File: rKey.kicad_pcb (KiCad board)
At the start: 2 copper layers, 52.8 x 71.4 mm, 38 parts, among them IC1 BDX34C, J1 Conn_01x06, Q1 BC337, Q2 BC337, Q3 BC337, Q4 BC337, Q5 BC327, Q8 BC337, U1 TL084BCN, U2 LM7810_TO220

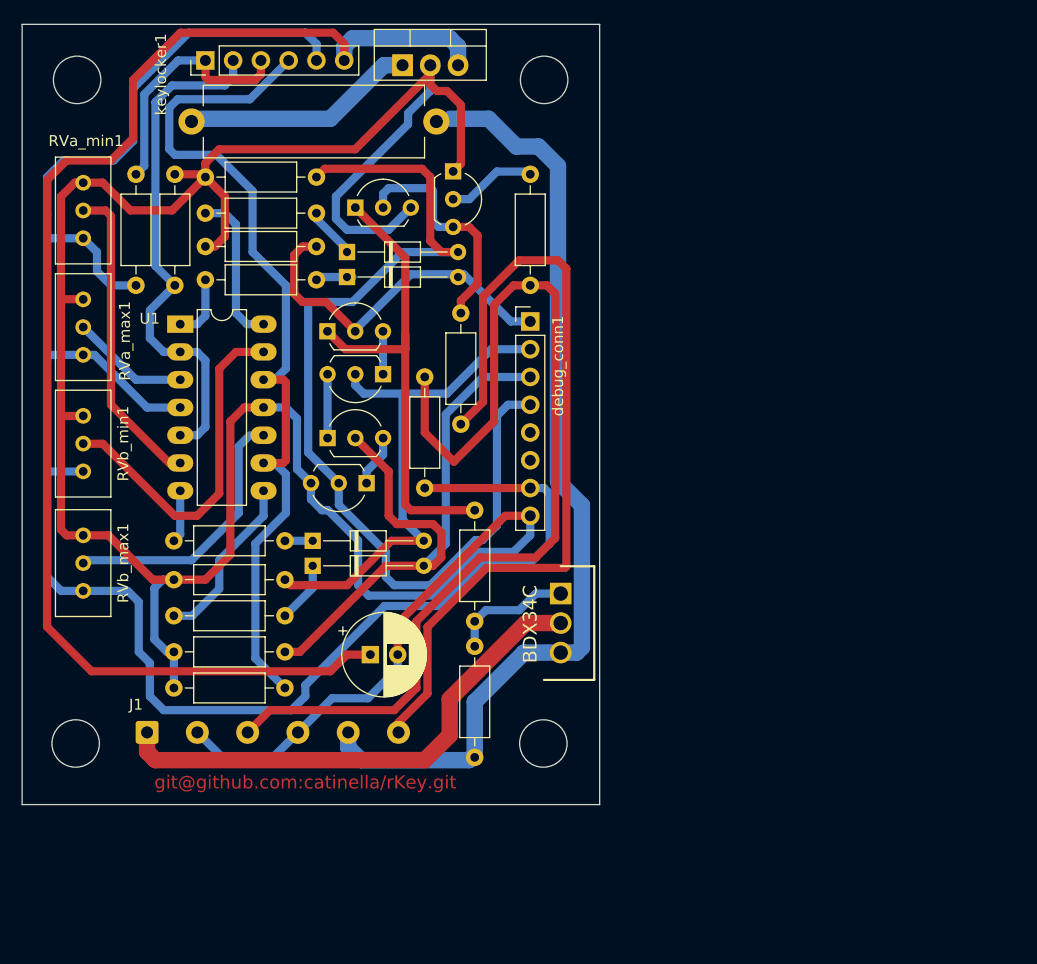
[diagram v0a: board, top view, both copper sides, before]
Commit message: Fix: Zenner diode added
To allow the STOP button to turn off the services' controller, the Zenner has been placed between the ON status holdon pin
and its BC327 transistor. When you stop the engine your key must be not plugged, obviosely.
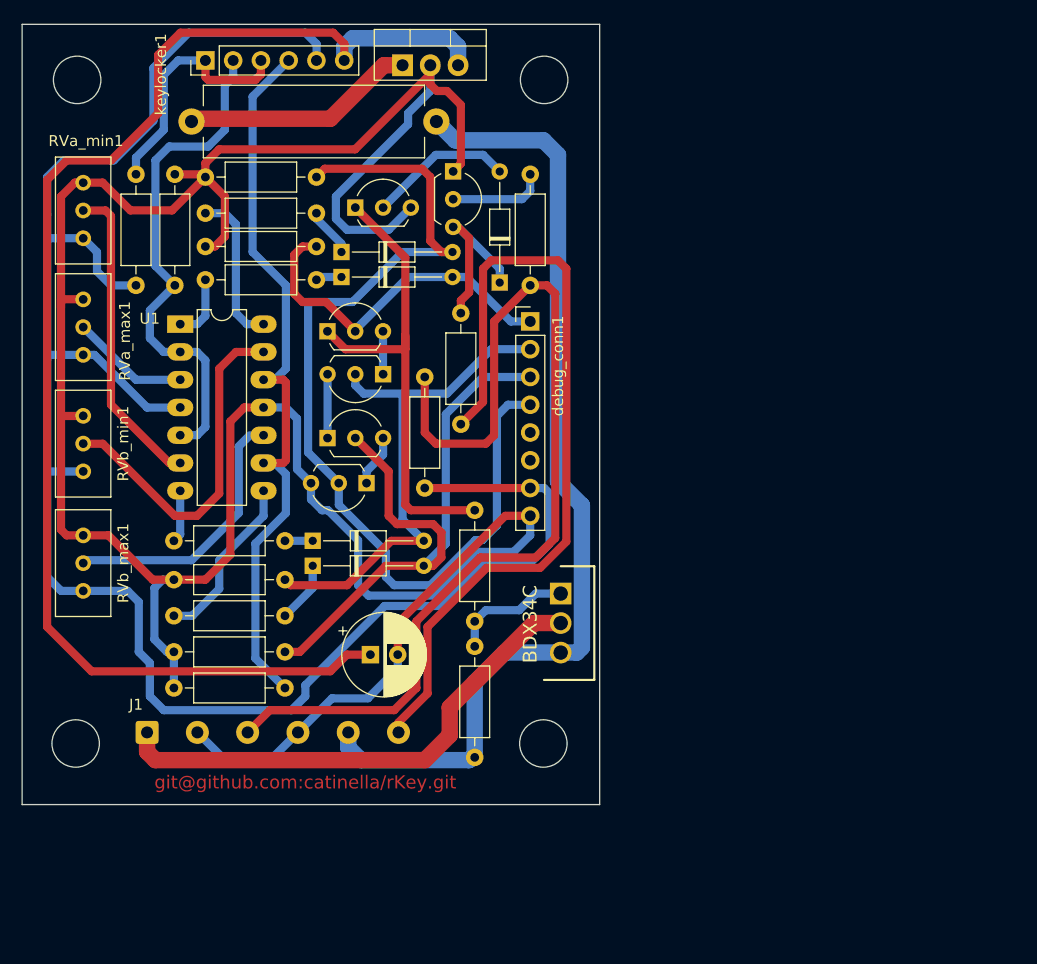
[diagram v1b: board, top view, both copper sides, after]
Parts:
- added ZD1: 2V, Diode_THT:D_DO-34_SOD68_P10.16mm_Horizontal, F.Cu at (160.3, 80.3)
- moved ZD4 0.51 mm to (145.8, 77.5)
- moved ZD5 0.51 mm to (145.8, 79.8)
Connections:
- Q5 pad 3: Net-(Q8-Pad2) -> Net-(R9-Pad1)
- R9 pad 1: Net-(Q8-Pad2) -> Net-(R9-Pad1)
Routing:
- net Net-(R9-Pad1): track 0.00 -> 16.2 mm
- net Net-(R8-Pad1): track 81.4 -> 69.0 mm
- net Net-(Q8-Pad2): track 21.3 -> 13.3 mm
- net Net-(IC1-Pad3): track 87.0 -> 89.7 mm
- net Net-(J1-Pad3): track 92.8 -> 91.3 mm
- net Net-(R2-Pad2): track 3.41 -> 2.39 mm
- net Net-(Q4-Pad2): track 89.8 -> 88.8 mm
- net Net-(R7-Pad1): track 47.5 -> 46.7 mm
- net Net-(R13-Pad1): track 8.21 -> 8.89 mm

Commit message: Release based on two D45VH10 (10A --> 3W) 2.5% wasted power
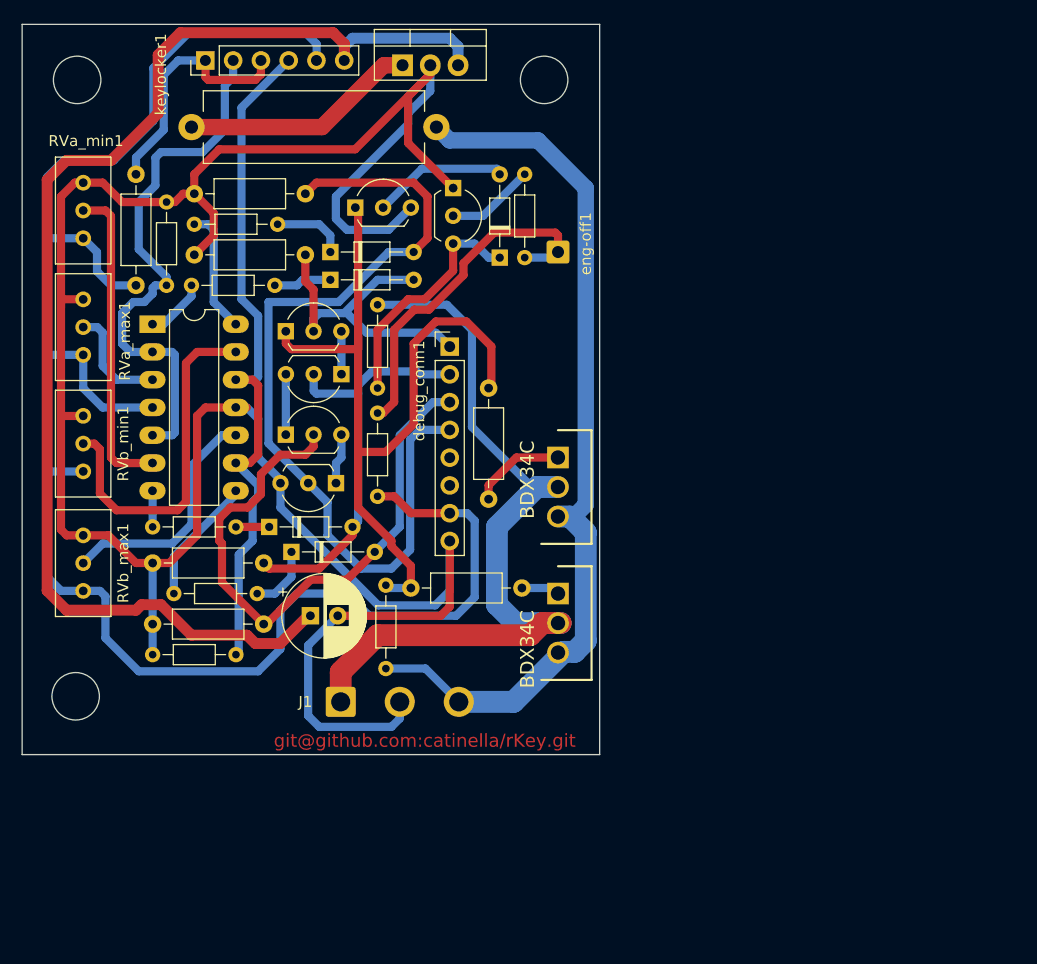
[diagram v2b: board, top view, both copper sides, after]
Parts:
- added IC2: BDX34C, BDX34C:TO270P460X1020X2008-3P, F.Cu at (165.6, 96.3)
- added R18: 1.6K, Resistor_THT:R_Axial_DIN0207_L6.3mm_D2.5mm_P10.16mm_Horizontal, F.Cu at (159.3, 89.9)
- added eng-off1: Conn_01x01, Connector_Wire:SolderWire-0.5sqmm_1x01_D0.9mm_OD2.1mm, F.Cu at (165.6, 77.5)
- J1: value Conn_01x06 -> Conn_01x03; footprint Connector_Wire:SolderWire-0.5sqmm_1x06_P4.6mm_D0.9mm_OD2.1mm -> Connector_Wire:SolderWire-1sqmm_1x03_P5.4mm_D1.4mm_OD2.7mm
- R10: value 5K -> 1.6K
- R11, R13, R14, R2, R3, R4, R5, R7, R8, R9: footprint Resistor_THT:R_Axial_DIN0207_L6.3mm_D2.5mm_P10.16mm_Horizontal -> Resistor_THT:R_Axial_DIN0204_L3.6mm_D1.6mm_P7.62mm_Horizontal
- ZD1, ZD2, ZD3, ZD4, ZD5: footprint Diode_THT:D_DO-34_SOD68_P10.16mm_Horizontal -> Diode_THT:D_DO-34_SOD68_P7.62mm_Horizontal
- moved J1 17.9 mm to (145.7, 118.6)
- moved R10 9.20 mm to (152.1, 108.2), turned to 0 degrees
- moved R11 8.38 mm to (149.9, 115.6), turned to 90 degrees
- moved debug_conn1 7.72 mm to (155.7, 86.1)
- moved R9 7.66 mm to (149.1, 82.3)
- moved C1 6.54 mm to (143.0, 110.7)
- moved R8 5.42 mm to (136.1, 114.3)
- moved R14 4.38 mm to (149.1, 99.8)
- moved ZD2 4.18 mm to (139.2, 102.6)
- moved Q3 3.83 mm to (140.7, 94.2)
- moved Q1 3.81 mm to (140.7, 84.7)
- moved Q2 3.81 mm to (145.8, 88.6)
- moved R16 3.20 mm to (128.5, 111.5)
- moved Q4 2.79 mm to (145.3, 98.6)
- moved U1 2.54 mm to (128.5, 84.1)
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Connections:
- IC1 pad 1: Net-(IC1-Pad1) -> Net-(R10-Pad2)
- IC1 pad 2: Net-(IC1-Pad2) -> Net-(J1-Pad1)
- J1 pad 1: Net-(IC1-Pad2) -> Net-(J1-Pad1)
- J1 pad 3: Net-(J1-Pad3) -> Net-(IC1-Pad3)
- Q1 pad 1: Net-(Q1-Pad1) -> Net-(R10-Pad1)
- Q5 pad 3: Net-(R9-Pad1) -> Net-(Q5-Pad3)
- Q8 pad 1: Net-(Q1-Pad1) -> Net-(R10-Pad1)
- R10 pad 1: Net-(Q1-Pad1) -> Net-(R10-Pad1)
- R10 pad 2: Net-(IC1-Pad1) -> Net-(R10-Pad2)
- R11 pad 1: Net-(IC1-Pad1) -> Net-(IC1-Pad3)
- R11 pad 2: Net-(IC1-Pad3) -> Net-(R10-Pad1)
- R13 pad 2: Net-(J1-Pad3) -> Net-(eng-off1-Pad1)
- R14 pad 2: Net-(J1-Pad3) -> Net-(eng-off1-Pad1)
- R9 pad 1: Net-(R9-Pad1) -> Net-(J1-Pad1)
- R9 pad 2: Net-(J1-Pad6) -> Net-(Q5-Pad3)
- ZD1 pad 1: Net-(R9-Pad1) -> Net-(Q5-Pad3)
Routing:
- net Net-(J1-Pad3): track 91.3 -> 0.00 mm
- net Net-(J1-Pad1): track 0.00 -> 75.4 mm
- net Net-(J1-Pad6): track 75.0 -> 0.00 mm
- net Net-(R10-Pad1): track 0.00 -> 74.7 mm
- net Net-(IC1-Pad2): track 46.6 -> 0.00 mm
- net Net-(Q1-Pad1): track 44.7 -> 0.00 mm
- net Net-(eng-off1-Pad1): track 0.00 -> 32.7 mm
- net GND: track 256.8 -> 234.6 mm
- net Net-(Q5-Pad3): track 0.00 -> 21.8 mm
- net Net-(R9-Pad1): track 16.2 -> 0.00 mm
- net Net-(R1-Pad1): track 179.0 -> 167.9 mm
- net Net-(IC1-Pad1): track 10.7 -> 0.00 mm
- net Net-(ZD2-Pad2): track 47.9 -> 38.2 mm
- net Net-(ZD4-Pad2): track 88.8 -> 80.1 mm
- net Net-(IC2-Pad1): track 0.00 -> 8.66 mm
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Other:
- board size 52.8 x 71.4 mm -> 52.8 x 66.8 mm

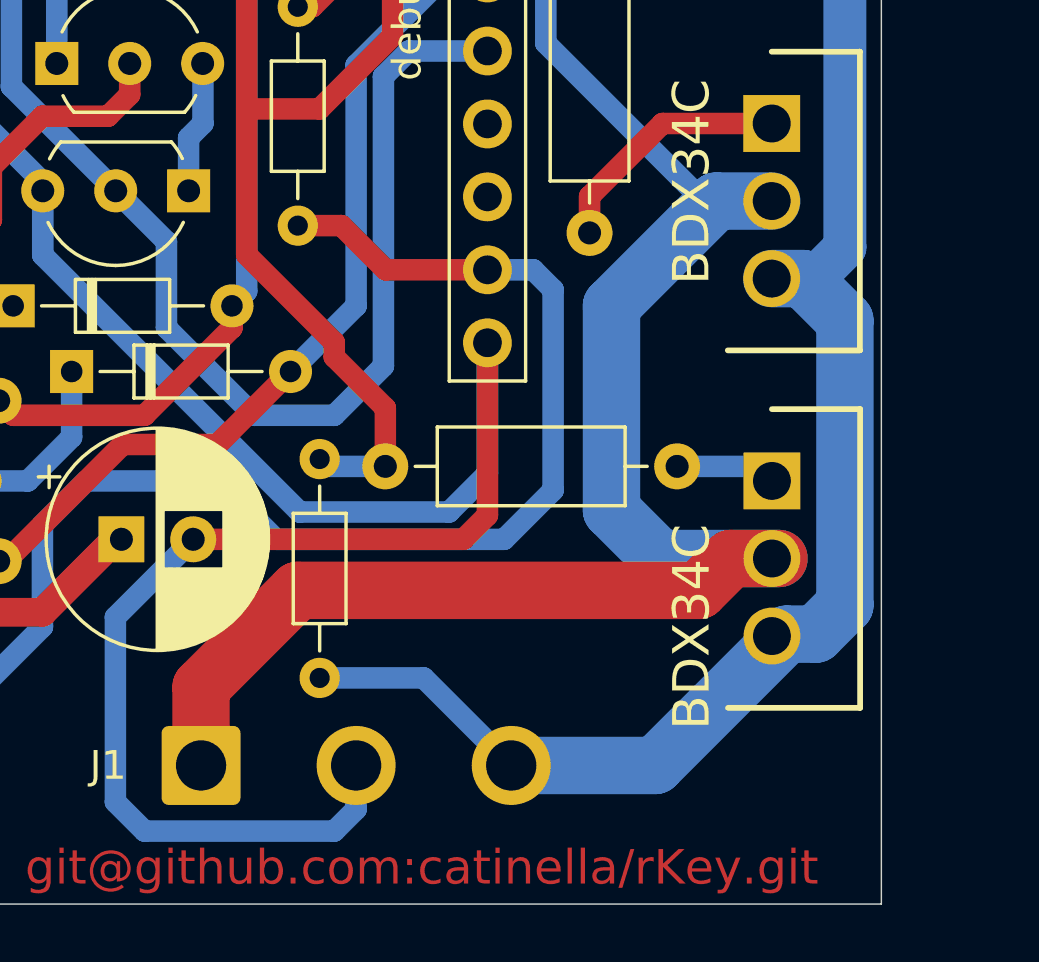
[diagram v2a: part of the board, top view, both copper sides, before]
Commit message: redundant links for high current (4mm track size virtually)
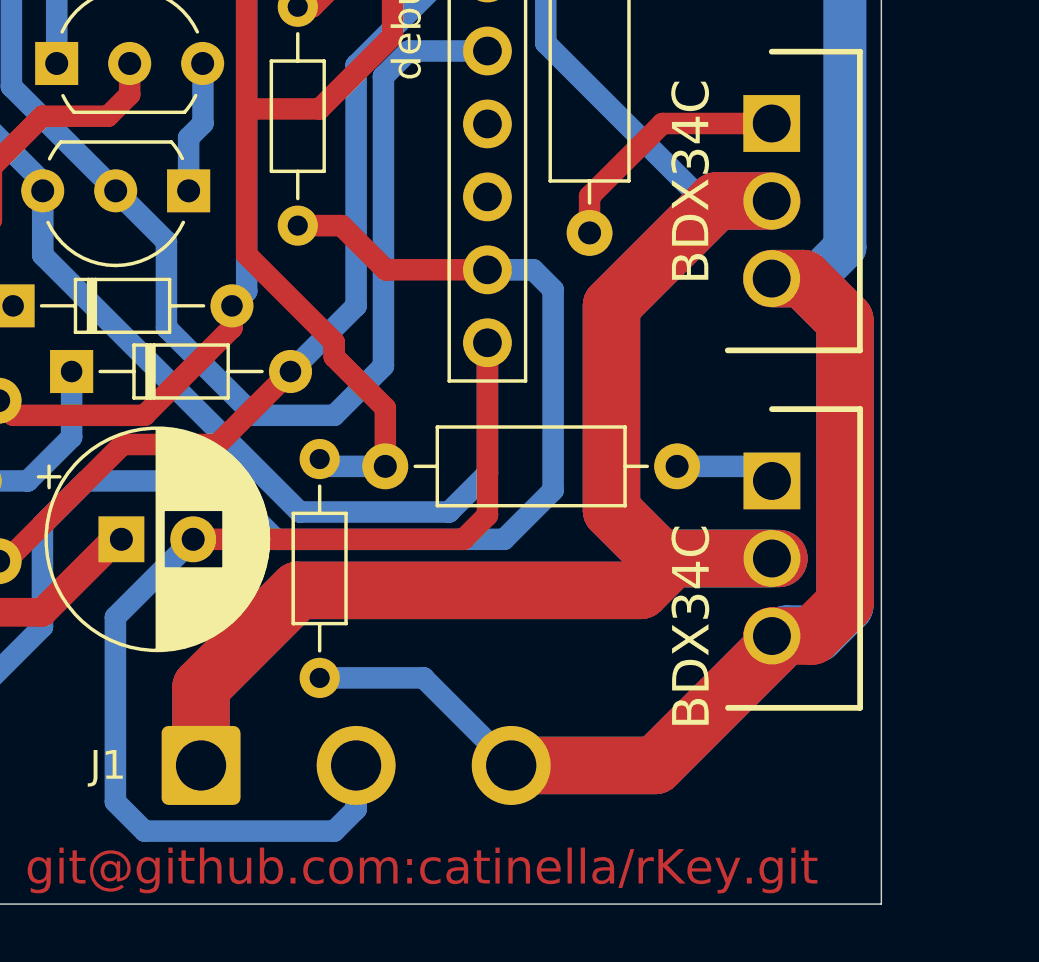
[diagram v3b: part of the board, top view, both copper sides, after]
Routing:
- net Net-(J1-Pad1): track 75.4 -> 119.3 mm
- net Net-(IC1-Pad3): track 82.9 -> 110.1 mm
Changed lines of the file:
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@@
   (segment (start 145.542 82.042) (end 139.126 82.042) (width 0.75) (layer "B.Cu") (net 20))
   (segment (start 152.08 104.714) (end 152.08 94.627502) (width 0.75) (layer "B.Cu") (net 20))
+  (segment (start 161.036 112.522) (end 149.098 112.522) (width 2) (layer "F.Cu") (net 21))
   (segment (start 149.098 112.522) (end 145.73 115.89) (width 2) (layer "F.Cu") (net 21))
-  (segment (start 163.068 112.522) (end 149.098 112.522) (width 2) (layer "F.Cu") (net 21))
-  (segment (start 164.178 111.412) (end 163.068 112.522) (width 2) (layer "F.Cu") (net 21))
-  (segment (start 165.854 111.412) (end 164.178 111.412) (width 2) (layer "F.Cu") (net 21))
-  (segment (start 165.854 111.412) (end 164.498 111.412) (width 1.5) (layer "F.Cu") (net 21))
+  (segment (start 165.854 111.412) (end 162.146 111.412) (width 2) (layer "F.Cu") (net 21))
+  (segment (start 160.02 102.616) (end 163.67 98.966) (width 2) (layer "F.Cu") (net 21))
   (segment (start 145.73 115.89) (end 145.73 118.618) (width 2) (layer "F.Cu") (net 21))
+  (segment (start 162.146 111.412) (end 161.036 112.522) (width 2) (layer "F.Cu") (net 21))
+  (segment (start 165.854 111.412) (end 161.704 111.412) (width 1.5) (layer "F.Cu") (net 21))
+  (segment (start 160.02 102.616) (end 160.02 109.728) (width 2) (layer "F.Cu") (net 21))
+  (segment (start 163.67 98.966) (end 165.6 98.966) (width 2) (layer "F.Cu") (net 21))
+  (segment (start 160.02 109.728) (end 161.704 111.412) (width 2) (layer "F.Cu") (net 21))
   (segment (start 163.228 98.966) (end 157.734 93.472) (width 0.75) (layer "B.Cu") (net 21))
+  (segment (start 149.098 112.522) (end 161.036 112.522) (width 2) (layer "B.Cu") (net 21))
   (segment (start 157.734 84.582) (end 155.448 82.296) (width 0.75) (layer "B.Cu") (net 21))
   (segment (start 165.6 98.966) (end 163.228 98.966) (width 0.75) (layer "B.Cu") (net 21))
+  (segment (start 145.73 115.89) (end 149.098 112.522) (width 2) (layer "B.Cu") (net 21))
   (segment (start 163.67 98.966) (end 160.02 102.616) (width 2) (layer "B.Cu") (net 21))
   (segment (start 160.02 102.616) (end 160.02 109.728) (width 2) (layer "B.Cu") (net 21))
   (segment (start 160.02 109.728) (end 161.704 111.412) (width 2) (layer "B.Cu") (net 21))
+  (segment (start 161.036 112.522) (end 162.146 111.412) (width 2) (layer "B.Cu") (net 21))
   (segment (start 165.6 98.966) (end 163.67 98.966) (width 2) (layer "B.Cu") (net 21))
+  (segment (start 162.146 111.412) (end 165.608 111.412) (width 2) (layer "B.Cu") (net 21))
   (segment (start 161.704 111.412) (end 165.854 111.412) (width 2) (layer "B.Cu") (net 21))
   (segment (start 155.448 82.296) (end 149.098 82.296) (width 0.75) (layer "B.Cu") (net 21))
   (segment (start 157.734 93.472) (end 157.734 84.582) (width 0.75) (layer "B.Cu") (net 21))
+  (segment (start 145.73 118.618) (end 145.73 115.89) (width 2) (layer "B.Cu") (net 21))
   (segment (start 137.145 96.769) (end 137.419 96.769) (width 0.75) (layer "F.Cu") (net 22))
   (segment (start 137.419 96.769) (end 138.176 96.012) (width 0.75) (layer "F.Cu") (net 22))
@@
   (segment (start 159.263 77.983) (end 157.978 76.698) (width 0.75) (layer "B.Cu") (net 33))
   (segment (start 160.274 77.983) (end 159.263 77.983) (width 0.75) (layer "B.Cu") (net 33))
+  (segment (start 165.608 114.554) (end 165.608 114.112) (width 2) (layer "F.Cu") (net 34))
+  (segment (start 165.608 114.112) (end 167.008071 114.112) (width 2) (layer "F.Cu") (net 34))
+  (segment (start 168.148 103.124) (end 166.69 101.666) (width 2) (layer "F.Cu") (net 34))
+  (segment (start 156.53 118.618) (end 161.544 118.618) (width 2) (layer "F.Cu") (net 34))
+  (segment (start 166.69 101.666) (end 165.6 101.666) (width 2) (layer "F.Cu") (net 34))
+  (segment (start 167.008071 114.112) (end 168.148 112.972071) (width 2) (layer "F.Cu") (net 34))
+  (segment (start 168.148 112.972071) (end 168.148 103.124) (width 2) (layer "F.Cu") (net 34))
+  (segment (start 161.544 118.618) (end 165.608 114.554) (width 2) (layer "F.Cu") (net 34))
   (segment (start 149.86 115.57) (end 153.482 115.57) (width 0.75) (layer "B.Cu") (net 34))
   (segment (start 168.148 103.124) (end 168.148 113.03) (width 2) (layer "B.Cu") (net 34))
